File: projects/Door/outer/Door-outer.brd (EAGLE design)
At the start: 48.3 x 30.5 mm, 14 parts

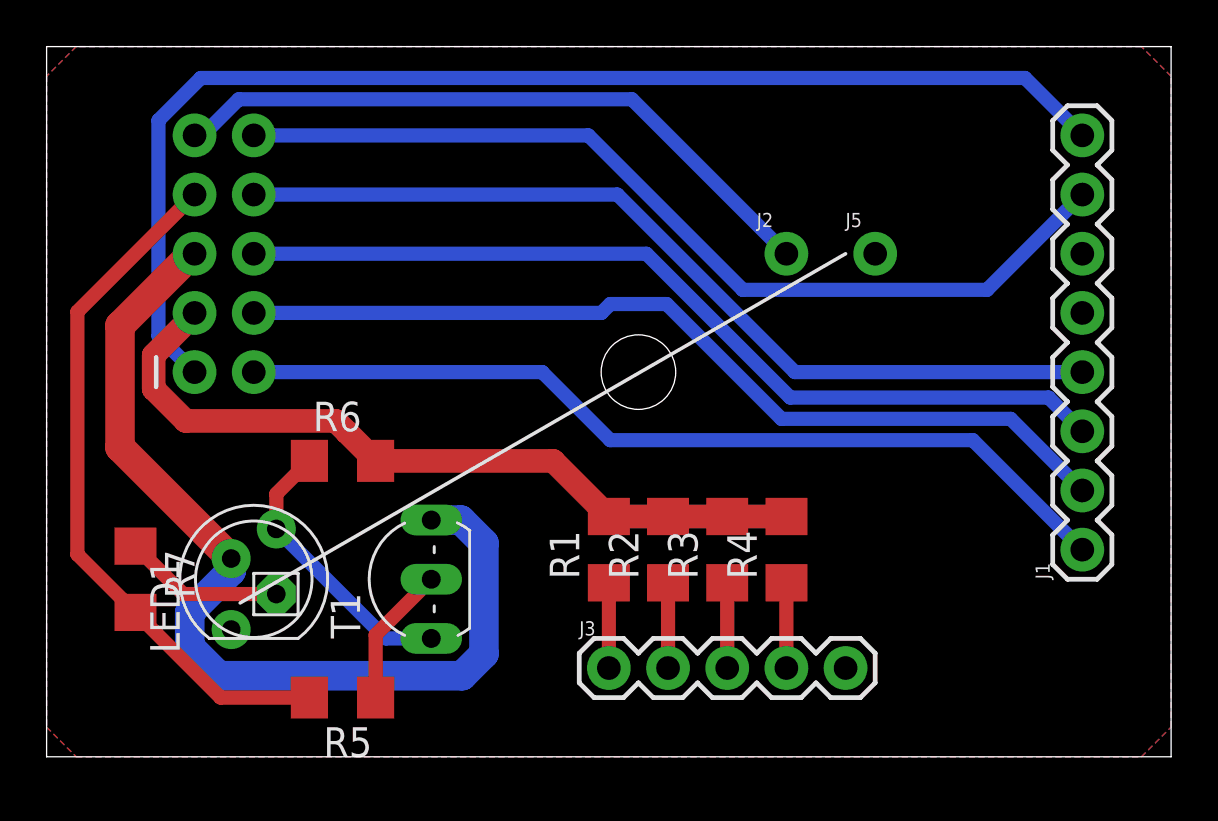
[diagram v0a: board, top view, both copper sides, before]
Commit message: Rerouted door boards for rivet-plated vias instead of plated through-holes
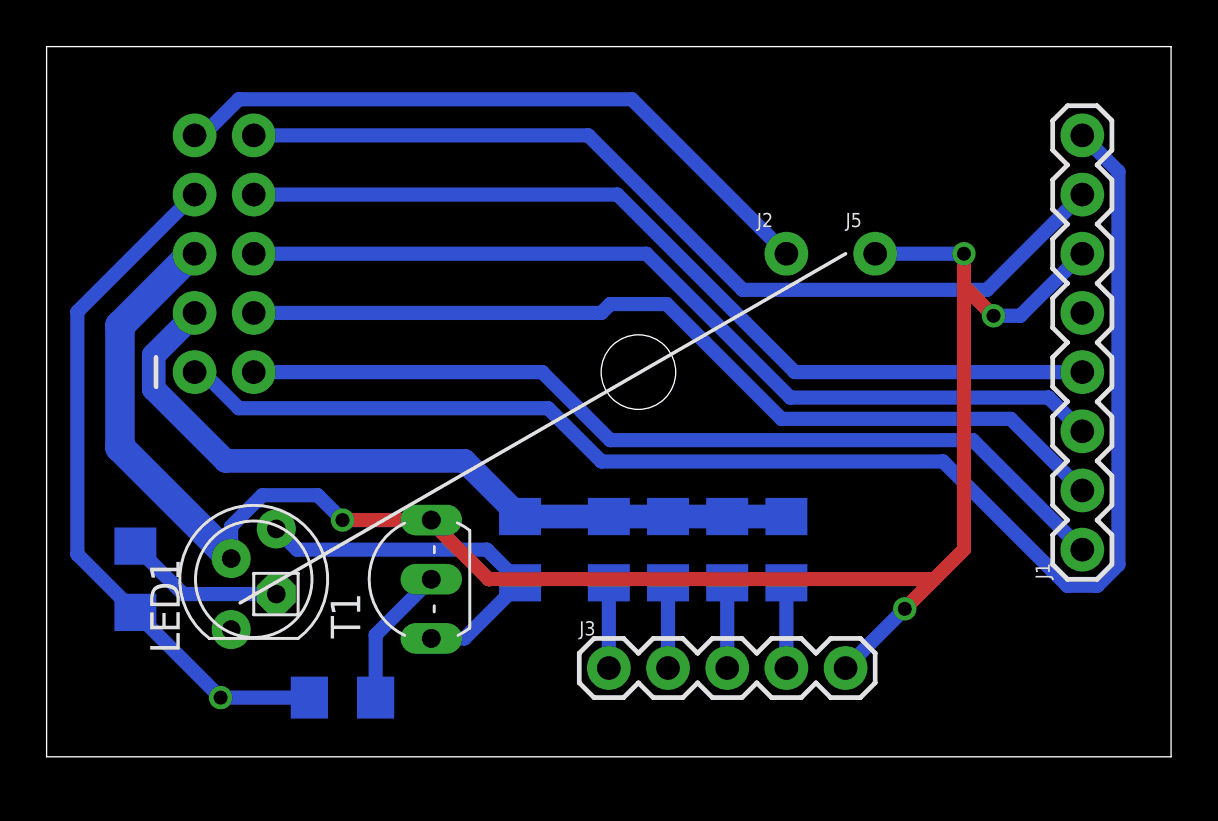
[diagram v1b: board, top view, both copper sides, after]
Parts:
- moved R6 8.52 mm to (22.9, 8.89), flipped to the bottom, turned to 90 degrees
- flipped R1 to the bottom
- flipped R2 to the bottom
- flipped R3 to the bottom
- flipped R4 to the bottom
- flipped R5 to the bottom, turned to 0 degrees
- flipped R7 to the bottom
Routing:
- net GND: track 41.9 -> 84.3 mm, vias 0 -> 4
- net +3V3: track 52.9 -> 62.9 mm
- net N$18: track 12.1 -> 16.2 mm
- net STATUS: vias 0 -> 1
- removed copper zone on layer 1, net GND
- removed copper zone on layer 16, net GND

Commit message: Via rivets apparently have a 0.6mm INNER diameter
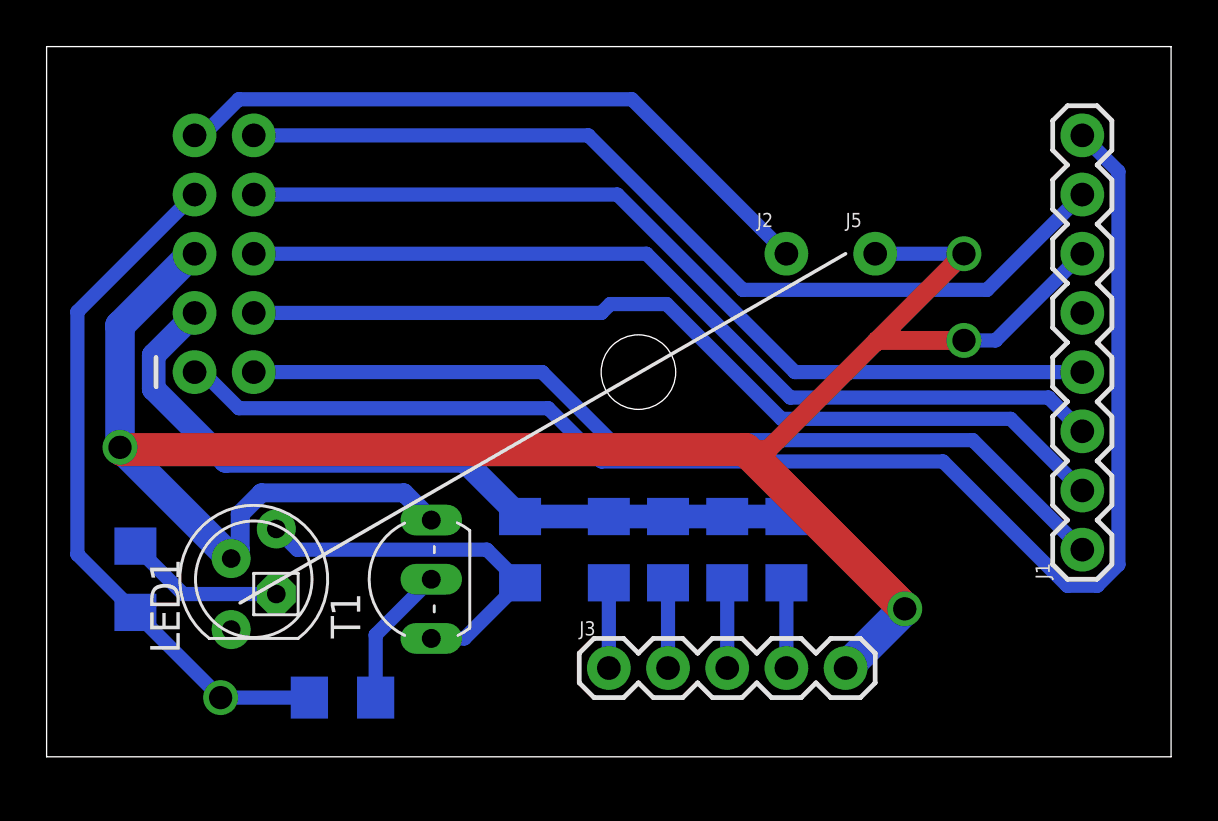
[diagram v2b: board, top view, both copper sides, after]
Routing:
- net GND: track 84.3 -> 94.7 mm
